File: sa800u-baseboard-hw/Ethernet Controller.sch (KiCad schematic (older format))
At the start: 33 parts, among them T1 749020010A, U1 RTL8111H

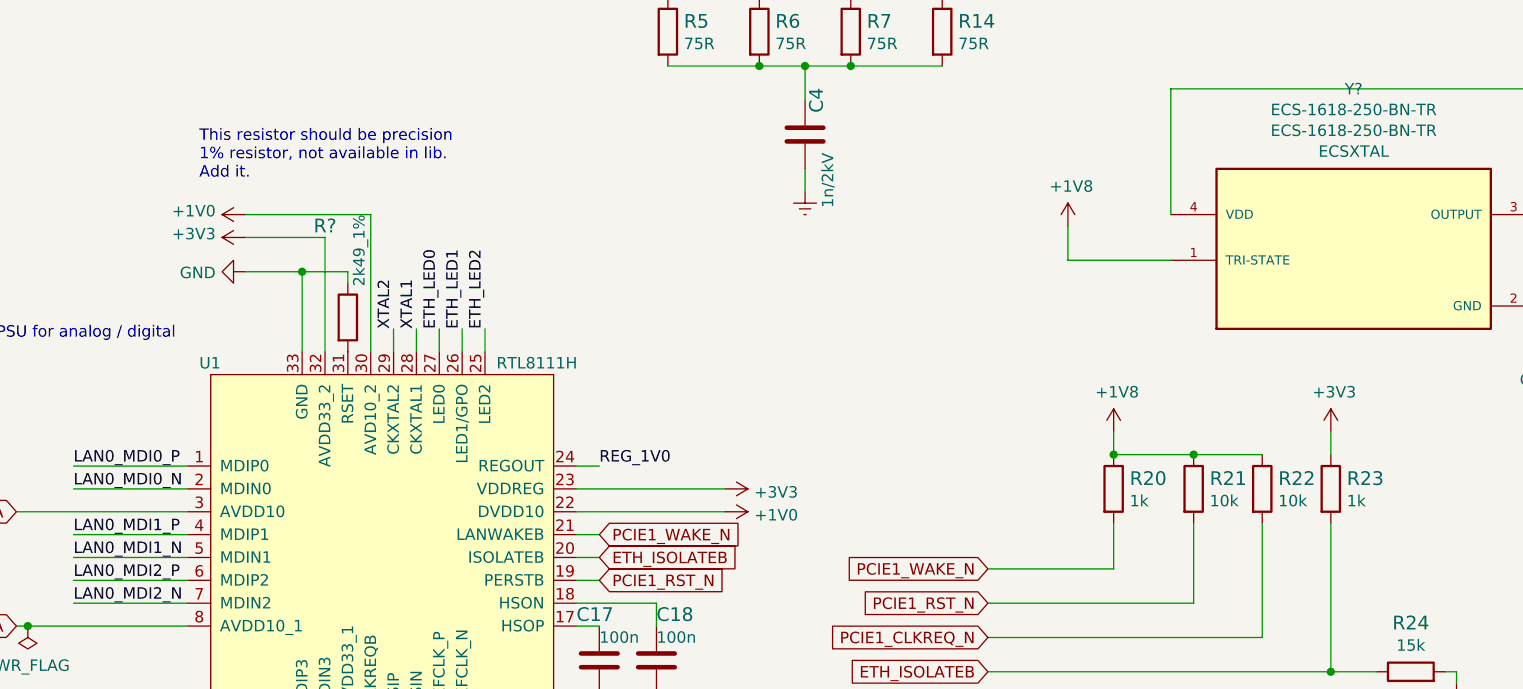
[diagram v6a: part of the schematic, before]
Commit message: fixed / unified power labels
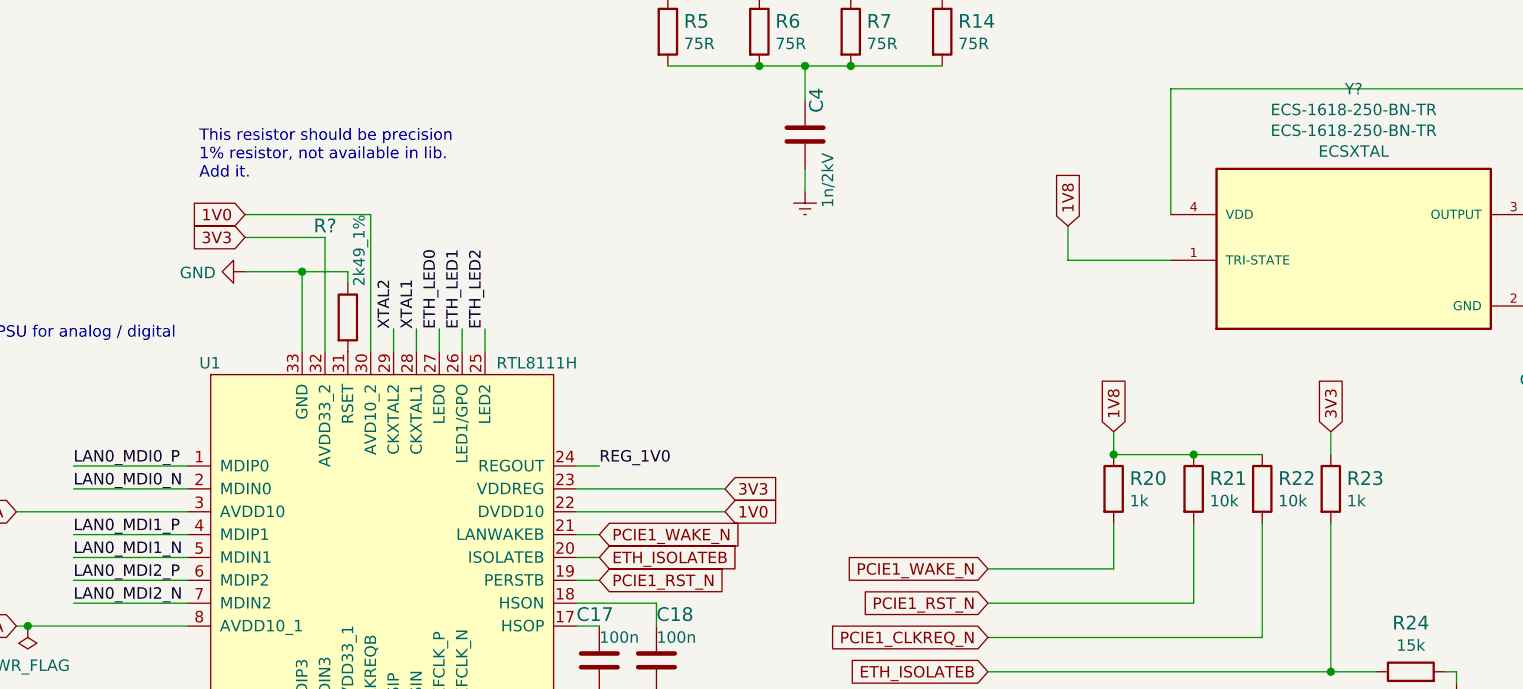
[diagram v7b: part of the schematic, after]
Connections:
- net +3V3 is gone; now on net 3V3: R23.1, U1.23 (VDDREG), U1.32 (AVDD33_2)
- net +1V0 renamed 1V0
- net +1V8 renamed 1V8
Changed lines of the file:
@@
 Wire Wire Line
 	4200 5600 4850 5600
-$Comp
-L power:+3V3 #PWR0107
-U 1 1 61B00EC4
-P 4850 5600
-F 0 "#PWR0107" H 4850 5450 50  0001 C CNN
-F 1 "+3V3" V 4865 5728 50  0000 L CNN
-F 2 "" H 4850 5600 50  0001 C CNN
-F 3 "" H 4850 5600 50  0001 C CNN
-	1    4850 5600
-	0    1    1    0
-$EndComp
-$Comp
-L power:+3V3 #PWR0108
-U 1 1 61B018F8
-P 2750 4500
-F 0 "#PWR0108" H 2750 4350 50  0001 C CNN
-F 1 "+3V3" V 2765 4628 50  0000 L CNN
-F 2 "" H 2750 4500 50  0001 C CNN
-F 3 "" H 2750 4500 50  0001 C CNN
-	1    2750 4500
-	0    -1   -1   0
-$EndComp
 Wire Wire Line
 	2750 4400 3300 4400
-$Comp
-L power:+1V0 #PWR0109
-U 1 1 61B052E9
-P 2750 4400
-F 0 "#PWR0109" H 2750 4250 50  0001 C CNN
-F 1 "+1V0" V 2765 4528 50  0000 L CNN
-F 2 "" H 2750 4400 50  0001 C CNN
-F 3 "" H 2750 4400 50  0001 C CNN
-	1    2750 4400
-	0    -1   -1   0
-$EndComp
-$Comp
-L power:+1V0 #PWR0110
-U 1 1 61B06D93
-P 4850 5700
-F 0 "#PWR0110" H 4850 5550 50  0001 C CNN
-F 1 "+1V0" V 4865 5828 50  0000 L CNN
-F 2 "" H 4850 5700 50  0001 C CNN
-F 3 "" H 4850 5700 50  0001 C CNN
-	1    4850 5700
-	0    1    1    0
-$EndComp
 Wire Wire Line
 	2050 1100 2800 1100
@@
 Wire Wire Line
 	6350 4600 6350 4450
-$Comp
-L power:+1V8 #PWR04
-U 1 1 61999203
-P 6350 4450
-F 0 "#PWR04" H 6350 4300 50  0001 C CNN
-F 1 "+1V8" H 6365 4623 50  0000 C CNN
-F 2 "" H 6350 4450 50  0001 C CNN
-F 3 "" H 6350 4450 50  0001 C CNN
-	1    6350 4450
-	1    0    0    -1
-$EndComp
 Wire Wire Line
 	8400 4800 8400 4950
@@
 F 3 "" H 8400 4950 50  0001 C CNN
 	1    8400 4950
-	1    0    0    -1
-$EndComp
-$Comp
-L power:+1V8 #PWR013
-U 1 1 619C44BD
-P 6550 5350
-F 0 "#PWR013" H 6550 5200 50  0001 C CNN
-F 1 "+1V8" H 6565 5523 50  0000 C CNN
-F 2 "" H 6550 5350 50  0001 C CNN
-F 3 "" H 6550 5350 50  0001 C CNN
-	1    6550 5350
 	1    0    0    -1
 $EndComp
@@
 Wire Wire Line
 	7500 5450 7500 5350
-$Comp
-L power:+3V3 #PWR014
-U 1 1 61A00249
-P 7500 5350
-F 0 "#PWR014" H 7500 5200 50  0001 C CNN
-F 1 "+3V3" H 7515 5523 50  0000 C CNN
-F 2 "" H 7500 5350 50  0001 C CNN
-F 3 "" H 7500 5350 50  0001 C CNN
-	1    7500 5350
-	1    0    0    -1
-$EndComp
 Wire Wire Line
 	7500 6400 7700 6400
@@
 	0    1    1    0
 $EndComp
+Text GLabel 2750 4500 0    50   Input ~ 0
+3V3
+Text GLabel 2750 4400 0    50   Input ~ 0
+1V0
+Text GLabel 4850 5600 2    50   Input ~ 0
+3V3
+Text GLabel 4850 5700 2    50   Input ~ 0
+1V0
+Text GLabel 6550 5350 1    50   Input ~ 0
+1V8
+Text GLabel 7500 5350 1    50   Input ~ 0
+3V3
+Text GLabel 6350 4450 1    50   Input ~ 0
+1V8
 $EndSCHEMATC

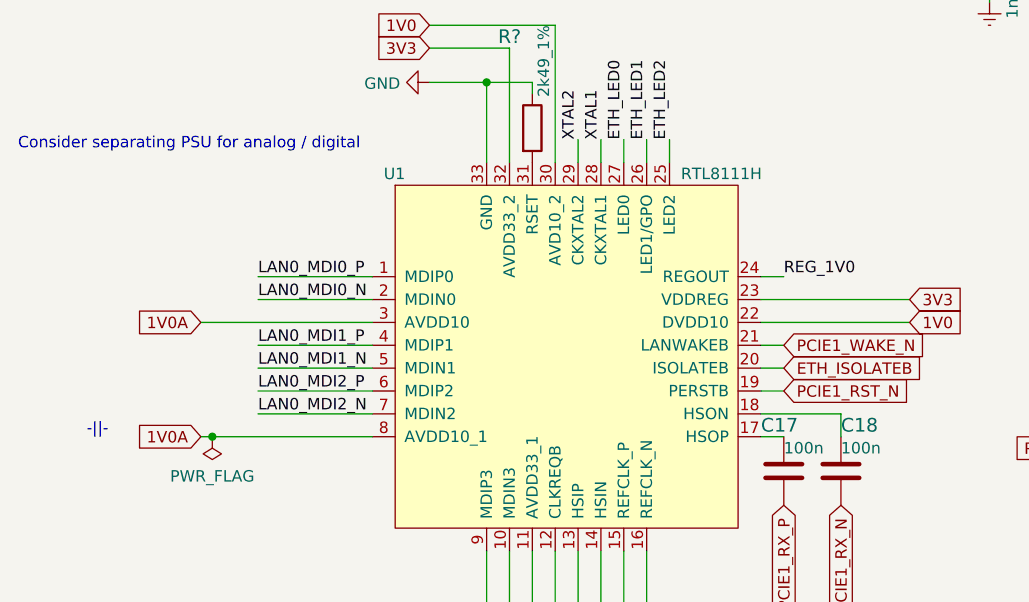
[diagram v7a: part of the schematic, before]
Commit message: flattenning directory
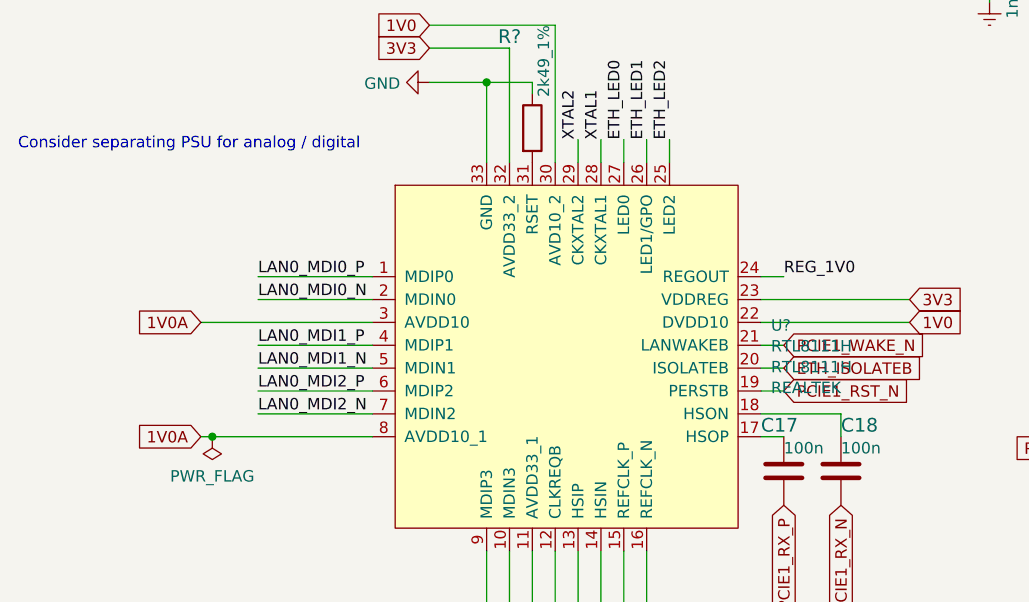
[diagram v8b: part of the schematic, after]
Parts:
- removed U1: RTL8111H, symbol RTL8111Hx:RTL8111H
- added U?: RTL8111H, antmicro-footprints:RTL8111H, symbol antmicroInterfaceControllers:RTL8111H
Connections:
- net 1V0: now also U?.22 (DVDD10), U?.30 (AVD10_2)
- net 1V0A: now also U?.3 (AVDD10), U?.8 (AVDD10_1)
- net 3V3: now also U?.11 (AVDD33_1), U?.23 (VDDREG), U?.32 (AVDD33_2)
- net ETH_ISOLATEB: now also U?.20 (ISOLATEB)
- net ETH_LED0: now also U?.27 (LED0)
- net ETH_LED1: now also U?.26 (LED1/GPO)
- net ETH_LED2: now also U?.25 (LED2)
- net GND: now also U?.33 (GND)
- net LAN0_MDI0_N: now also U?.2 (MDIN0)
- net LAN0_MDI0_P: now also U?.1 (MDIP0)
- net LAN0_MDI1_N: now also U?.5 (MDIN1)
- net LAN0_MDI1_P: now also U?.4 (MDIP1)
- net LAN0_MDI2_N: now also U?.7 (MDIN2)
- net LAN0_MDI2_P: now also U?.6 (MDIP2)
- net LAN0_MDI3_N: now also U?.10 (MDIN3)
- net LAN0_MDI3_P: now also U?.9 (MDIP3)
- net PCIE1_CLKREQ_N: now also U?.12 (CLKREQB)
- net PCIE1_REFCLK_N: now also U?.16 (REFCLK_N)
- net PCIE1_REFCLK_P: now also U?.15 (REFCLK_P)
- net PCIE1_RST_N: now also U?.19 (PERSTB)
- net PCIE1_TX_N: now also U?.14 (HSIN)
- net PCIE1_TX_P: now also U?.13 (HSIP)
- net PCIE1_WAKE_N: now also U?.21 (LANWAKEB)
- net REG_1V0: now also U?.24 (REGOUT)
- net XTAL1: now also U?.28 (CKXTAL1)
- net XTAL2: now also U?.29 (CKXTAL2)
- net at C17.2: now also U?.17 (HSOP)
- net at C18.2: now also U?.18 (HSON)
- net at R?.2: now also U?.31 (RSET)
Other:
- note removed: "-||-\n"
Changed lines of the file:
@@
 Comment4 ""
 $EndDescr
-Text Notes 1250 6200 0    50   ~ 0
--||-\n
 $Comp
 L antmicroInterfaceDriversReceiversTransceivers:749020010A T1
@@
 Text Label 3000 7400 1    50   ~ 0
 LAN0_MDI3_P
-$Comp
-L RTL8111Hx:RTL8111H U1
-U 1 1 618E8CA2
-P 2600 5100
-F 0 "U1" H 2550 5150 50  0000 L CNN
-F 1 "RTL8111H" H 3850 5150 50  0000 L CNN
-F 2 "" H 2500 4800 50  0001 C CNN
-F 3 "" H 2500 4800 50  0001 C CNN
-	1    2600 5100
-	1    0    0    -1
-$EndComp
 Wire Wire Line
 	2500 5800 2000 5800
@@
 Text GLabel 6350 4450 1    50   Input ~ 0
 1V8
+$Comp
+L antmicroInterfaceControllers:RTL8111H U?
+U 1 1 61A1B9F8
+P 2600 5100
+F 0 "U?" H 4244 4487 50  0000 L CNN
+F 1 "RTL8111H" H 4244 4396 50  0000 L CNN
+F 2 "antmicro-footprints:RTL8111H" H 2600 5100 50  0001 C CNN
+F 3 "" H 2600 5100 50  0001 C CNN
+F 4 "RTL8111H" H 4244 4305 50  0000 L CNN "MPN"
+F 5 "REALTEK" H 4244 4214 50  0000 L CNN "Manufacturer"
+	1    2600 5100
+	1    0    0    -1
+$EndComp
 $EndSCHEMATC
